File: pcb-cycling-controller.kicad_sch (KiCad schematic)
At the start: 46 parts, among them J1 Conn_01x02, J2 USB_C_Receptacle_USB2.0_16P, J3 Conn_01x06, Q1 SI2301CDS-T1-GE3-ES, Q2 SI2301CDS-T1-GE3-ES, SW1 SS12F44G4, U3 L7805, U4 MT3410LB

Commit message: Add details to the design
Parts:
- removed R14, R15, R37: 0, Resistor_SMD:R_0603_1608Metric, symbol Device:R_US
- removed U3: L7805, Package_TO_SOT_SMD:TO-263-2, symbol Regulator_Linear:L7805
- added C33: 22uF 10V, Capacitor_SMD:C_0603_1608Metric, symbol Device:C
- added C34: 0.1uF, Capacitor_SMD:C_0402_1005Metric, symbol Device:C
- added C9: 1uF, Capacitor_SMD:C_0603_1608Metric, symbol Device:C
- added D8: A7, Diode_SMD:D_SOD-123F, symbol Device:D_Filled
- added R38, R39, R40: 0, Resistor_SMD:R_0603_1608Metric, symbol Device:R_US
- added U3, U6: AMS1117-5.0, Package_TO_SOT_SMD:SOT-223-3_TabPin2, symbol Regulator_Linear:AMS1117-5.0
- J1: value Conn_01x02 -> Power; footprint Connector_PinHeader_2.54mm:PinHeader_1x02_P2.54mm_Vertical -> Connector_Molex:Molex_KK-254_AE-6410-02A_1x02_P2.54mm_Vertical; LCSC Part # (none) -> C27543
- J2: value USB_C_Receptacle_USB2.0_16P -> USB
- J3: value Conn_01x06 -> PROG
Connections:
- net BUCK_VIN: now also D8.1 (K)
- net GND: now also C33.1, C34.2, C9.2, U3.1 (GND), U6.1 (GND)
- net VBAT_SW: now also C9.1, U3.3 (VI), U6.3 (VI)
- net at J2.A4 (VBUS), J2.A9 (VBUS), J2.B4 (VBUS)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: now also D8.2 (A)
- net +5V: no longer names the net of C14.2, C15.1
- net +5V: now also R38.1, U3.2 (VO)
- new net: C33.2, C34.1, R39.1, U6.2 (VO)
- new net VLED1: R38.2, R40.2
- new net VLED2: R39.2, R40.1
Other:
- note added: "2S Li-Ion Battery 6.0-8.4V"
- note added: "Assume 100mA per strip"
- note added: "Powers +3.3V rail (but not LEDs) for development"
- note added: "Regulated LED Supplies"
- note added: "TODO: Regulator needs to support more voltage"
- note removed: "4xAA Battery 4.0-6.5V"
- note removed: "Populate R37 to power circuit via USB for development"
- note removed: "Provision for using different supplies for VLED"
- note removed: "Regulated LED Supply"
- note removed: "Regulates when Vbat > 5V Pass thru when Vbat < 5V"
- note removed: "TODO: This probably needs more current capability"

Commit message: Release candidate draft
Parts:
- removed C33: 22uF 10V, Capacitor_SMD:C_0603_1608Metric, symbol Device:C
- removed C34: 0.1uF, Capacitor_SMD:C_0402_1005Metric, symbol Device:C
- removed C9: 1uF, Capacitor_SMD:C_0603_1608Metric, symbol Device:C
- removed R38, R39, R40: 0, Resistor_SMD:R_0603_1608Metric, symbol Device:R_US
- removed U4: MT3410LB, Package_TO_SOT_SMD:SOT-23-5, symbol Regulator_Switching:NCP1529A
- removed U6: AMS1117-5.0, Package_TO_SOT_SMD:SOT-223-3_TabPin2, symbol Regulator_Linear:AMS1117-5.0
- added C38: 22nF, Capacitor_SMD:C_0603_1608Metric, symbol Device:C
- added H3, H4: MountingHole, MountingHole:MountingHole_2.2mm_M2_ISO7380_Pad, symbol Mechanical:MountingHole_Pad
- added U4: TX4113, Package_TO_SOT_SMD:SOT-23-6, symbol jlcpcb:TX4113
- FID1, FID2, FID3: footprint Fiducial:Fiducial_1mm_Mask3mm -> Fiducial:Fiducial_1mm_Mask2mm
- J3: now not fitted
- SW1: footprint mpn_footprints:SS12F44G4 -> MPN:SS12F44G4
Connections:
- net BUCK_FB: now also U4.3 (FB)
- net BUCK_VIN: now also U4.4 (EN), U4.5 (VIN)
- net GND: now also U4.2 (GND)
- net VLED: now reaches C14.2, C15.1, U3.2 (VO)
- net at L1.1: now also C38.1, U4.6 (SW)
- new net: C38.2, U4.1 (BS)
- no-connect marks 4 -> 6
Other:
- note added: "+3.3V Power Supply ~120mA"
- note added: "270mA Max"
- note added: "Regulated LED Supply"
- note removed: "+3.3V Power Supply ~120mA ESP32 + RTC"
- note removed: "Assume 100mA per strip"
- note removed: "Regulated LED Supplies"
- note removed: "TODO: Regulator needs to support more voltage"
- moved on the sheet: C14, C15, C17, C18, C19, C20, C8, FID1, FID2, FID3, L1, R16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

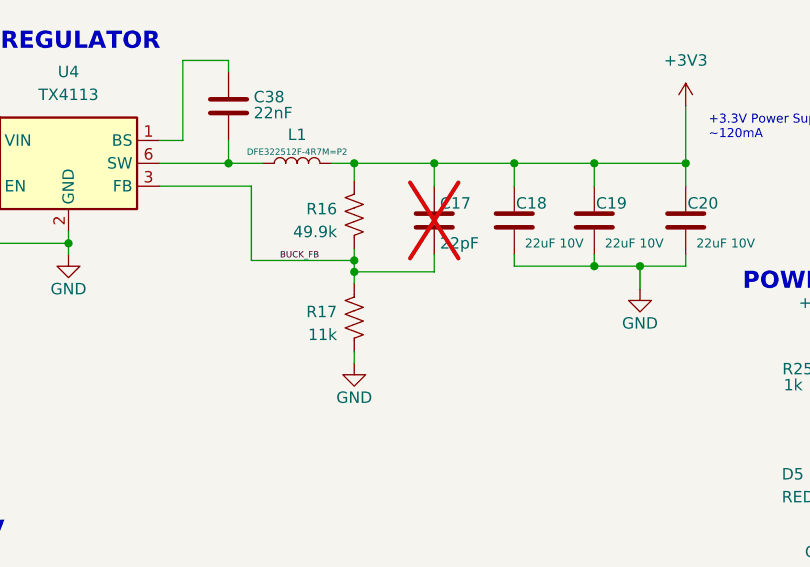
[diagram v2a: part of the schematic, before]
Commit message: Fix +3.3V reg fb resistor values
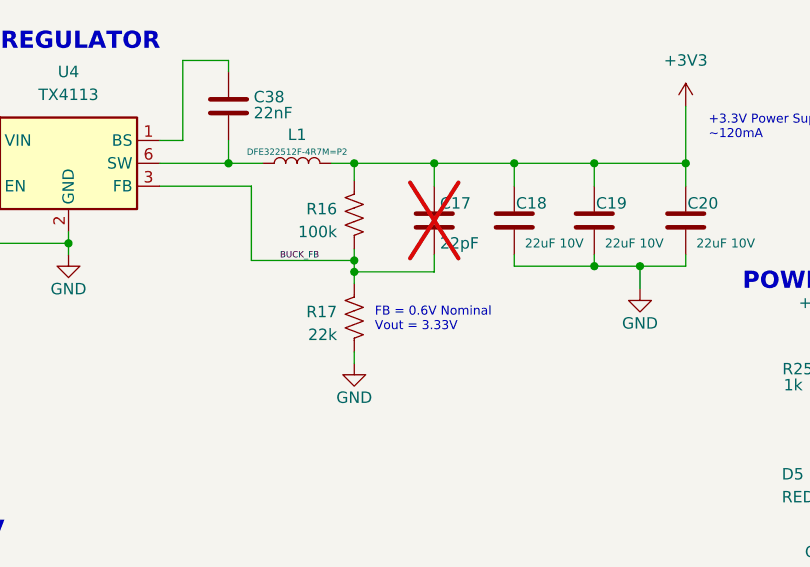
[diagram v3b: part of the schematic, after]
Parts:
- R16: value 49.9k -> 100k; LCSC Part # C23184 -> C25803
- R17: value 11k -> 22k; LCSC Part # C25950 -> C31850
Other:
- note added: "FB = 0.6V Nominal Vout = 3.33V"
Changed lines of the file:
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@@
 		)
 	)
+	(text "FB = 0.6V Nominal\nVout = 3.33V"
+		(exclude_from_sim no)
+		(at 204.216 54.356 0)
+		(effects
+			(font
+				(size 1 1)
+			)
+			(justify left bottom)
+		)
+	)
 	(junction
 		(at 151.765 33.02)
@@
 			)
 		)
-		(property "Value" "49.9k"
+		(property "Value" "100k"
 			(at 200.025 43.18 0)
 			(show_name no)
@@
 			)
 		)
-		(property "Datasheet" "https://datasheet.lcsc.com/lcsc/2206010116_UNI-ROYAL-Uniroyal-Elec-0603WAF4992T5E_C23184.pdf"
+		(property "Datasheet" ""
 			(at 201.93 41.275 0)
 			(hide yes)
@@
 			)
 		)
-		(property "LCSC Part #" "C23184"
+		(property "LCSC Part #" "C25803"
 			(at 201.93 41.275 0)
 			(hide yes)
@@
 			)
 		)
-		(property "Value" "11k"
+		(property "Value" "22k"
 			(at 200.025 54.61 0)
 			(show_name no)
@@
 			)
 		)
-		(property "Datasheet" "https://www.lcsc.com/datasheet/lcsc_datasheet_2206010045_UNI-ROYAL-Uniroyal-Elec-0603WAF1102T5E_C25950.pdf"
+		(property "Datasheet" ""
 			(at 201.93 52.705 0)
 			(hide yes)
@@
 			)
 		)
-		(property "LCSC Part #" "C25950"
+		(property "LCSC Part #" "C31850"
 			(at 201.93 52.705 0)
 			(hide yes)

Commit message: Address design review feedback
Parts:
- added F1: 1.5A, Fuse:Fuse_1812_4532Metric, symbol Device:Polyfuse
- J1: footprint Connector_Molex:Molex_KK-254_AE-6410-02A_1x02_P2.54mm_Vertical -> jlcpcb:CONN-TH_KF2510-2AW; LCSC Part # C27543 -> C30436
- R10: value 11k -> 22k; LCSC Part # C25950 -> C31850
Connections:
- net VBAT: now also F1.2; no longer J1.1 (Pin_1)
- new net: F1.1, J1.1 (Pin_1)
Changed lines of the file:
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@@
 	(wire
 		(pts
-			(xy 22.86 35.56) (xy 24.13 35.56)
+			(xy 22.86 35.56) (xy 25.4 35.56)
 		)
 		(stroke
@@
 	(wire
 		(pts
-			(xy 24.13 33.02) (xy 24.13 35.56)
+			(xy 38.1 33.02) (xy 38.1 35.56)
 		)
 		(stroke
@@
 	(wire
 		(pts
+			(xy 33.02 35.56) (xy 38.1 35.56)
+		)
+		(stroke
+			(width 0)
+			(type default)
+		)
+	)
+	(wire
+		(pts
 			(xy 66.04 41.91) (xy 66.04 33.02)
 		)
@@
 			)
 		)
-		(property "Value" "11k"
+		(property "Value" "22k"
 			(at 114.935 42.545 0)
 			(show_name no)
@@
 			)
 		)
-		(property "LCSC Part #" "C25950"
+		(property "LCSC Part #" "C31850"
 			(at 113.03 40.64 0)
 			(hide yes)
@@
 	(symbol
 		(lib_id "power:+12V")
-		(at 24.13 33.02 0)
+		(at 38.1 33.02 0)
 		(unit 1)
 		(body_style 1)
@@
 		(dnp no)
 		(property "Reference" "#PWR01"
-			(at 24.13 36.83 0)
+			(at 38.1 36.83 0)
 			(hide yes)
 			(show_name no)
@@
 		)
 		(property "Value" "VBAT"
-			(at 24.13 29.464 0)
+			(at 38.1 29.464 0)
 			(show_name no)
 			(do_not_autoplace no)
@@
 		)
 		(property "Footprint" ""
-			(at 24.13 33.02 0)
+			(at 38.1 33.02 0)
 			(hide yes)
 			(show_name no)
@@
 		)
 		(property "Datasheet" ""
-			(at 24.13 33.02 0)
+			(at 38.1 33.02 0)
 			(hide yes)
 			(show_name no)
@@
 		)
 		(property "Description" "Power symbol creates a global label with name \"+12V\""
-			(at 24.13 33.02 0)
+			(at 38.1 33.02 0)
 			(hide yes)
 			(show_name no)
@@
 			)
 		)
-		(property "Footprint" "Connector_Molex:Molex_KK-254_AE-6410-02A_1x02_P2.54mm_Vertical"
+		(property "Footprint" "jlcpcb:CONN-TH_KF2510-2AW"
 			(at 17.78 35.56 0)
 			(hide yes)
@@
 			)
 		)
-		(property "LCSC Part #" "C27543"
+		(property "LCSC Part #" "C30436"
 			(at 17.78 35.56 0)
 			(hide yes)
@@
 					(unit 1)
 				)
+			)
+		)
+	)
+	(symbol
+		(lib_id "Device:Polyfuse")
+		(at 29.21 35.56 90)
+		(unit 1)
+		(body_style 1)
+		(exclude_from_sim no)
+		(in_bom yes)
+		(on_board yes)
+		(in_pos_files yes)
+		(dnp no)
+		(property "Reference" "F1"
+			(at 25.654 33.528 90)
+			(show_name no)
+			(do_not_autoplace no)
+			(effects
+				(font
+					(size 1.27 1.27)
+				)
+			)
+		)
+		(property "Value" "1.5A"
+			(at 34.544 33.528 90)
+			(show_name no)
+			(do_not_autoplace no)
+			(effects
+				(font
+					(size 1.27 1.27)
+				)
+			)
+		)
+		(property "Footprint" "Fuse:Fuse_1812_4532Metric"
+			(at 34.29 34.29 0)
+			(hide yes)
+			(show_name no)
+			(do_not_autoplace no)
+			(effects
+				(font
+					(size 1.27 1.27)
+				)
+				(justify left)
+			)
+		)
+		(property "Datasheet" ""
+			(at 29.21 35.56 0)
+			(hide yes)
+			(show_name no)
+			(do_not_autoplace no)
+			(effects
+				(font
+					(size 1.27 1.27)
+				)
+			)
+		)
+		(property "Description" "Resettable fuse, polymeric positive temperature coefficient"
+			(at 29.21 35.56 0)
+			(hide yes)
+			(show_name no)
+			(do_not_autoplace no)
+			(effects
+				(font
+					(size 1.27 1.27)
+				)
+			)
+		)
+		(property "LCSC" "C883153"
+			(at 29.21 35.56 90)
+			(hide yes)
+			(show_name no)
+			(do_not_autoplace no)
+			(effects
+				(font
+					(size 1.27 1.27)
+				)
+			)
+		)
+		(property "LCSC Part #" "C883153"
+			(at 29.21 35.56 90)
+			(hide yes)
+			(show_name no)
+			(do_not_autoplace no)
+			(effects
+				(font
+					(size 1.27 1.27)
+				)
+			)
+		)
+		(pin "2"
+		)
+		(pin "1"
+		)
+		(instances
+			(project "pcb-cycling-controller"
+				(path "/ffeade77-fbf5-4d3a-8052-ea27942d440a"
+					(reference "F1")
+					(unit 1)
+				)
